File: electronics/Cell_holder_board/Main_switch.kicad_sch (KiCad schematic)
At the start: 0 parts

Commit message: Wiring diagram for mainswitch done
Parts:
- added BT5: Battery_Cell, symbol Device:Battery_Cell
- added Q1, Q2: IRLB8721PBF, Package_TO_SOT_THT:TO-220-3_Vertical, symbol Transistor_FET:IRLB8721PBF
- added R1: 1k, symbol Device:R
- added R2: 47k, symbol Device:R
- added R3: 4.7k, symbol Device:R
- added U1: LTV-817, Package_DIP:DIP-4_W7.62mm, symbol Isolator:LTV-817
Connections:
- new net: Q1.1 (G), Q2.1 (G), R2.1, U1.3
- new net: Q1.3 (S), Q2.3 (S), R2.2
- new net: R3.2, U1.2
- new net: R1.2, U1.4
- new net Arduino_mainswitch_gpio: U1.1
- new net GND: BT5.2 (-), Q1.2 (D), R3.1
- new net Load_minus: Q2.2 (D)
- new net Load_plus: BT5.1 (+), R1.1

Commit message: discord session with Johannes and Fabian, Schematic nearly done, all footprints fields filled
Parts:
- removed BT5: Battery_Cell, symbol Device:Battery_Cell
- added D1: 20V, Diode_SMD:D_SMA, symbol Device:D_TVS
- R1, R2, R3: footprint (none) -> Resistor_SMD:R_0805_2012Metric
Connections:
- net GND: now also D1.2 (A2)
- net Load_minus renamed Switch
- net Switch: now also D1.1 (A1)
- net Load_plus renamed U_Batt
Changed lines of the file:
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@@
 (kicad_sch (version 20230121) (generator eeschema)
   (paper "A4")
-  (junction (at 139.7 54.61) (diameter 0) (color 0 0 0 0)
-  )
   (junction (at 111.76 69.85) (diameter 0) (color 0 0 0 0)
   )
-  (junction (at 182.88 54.61) (diameter 0) (color 0 0 0 0)
+  (junction (at 139.7 93.98) (diameter 0) (color 0 0 0 0)
   )
   (junction (at 111.76 78.74) (diameter 0) (color 0 0 0 0)
   )
+  (junction (at 139.7 64.77) (diameter 0) (color 0 0 0 0)
+  )
   (junction (at 139.7 78.74) (diameter 0) (color 0 0 0 0)
   )
-  (wire (pts (xy 139.7 93.98) (xy 139.7 113.03))
-    (stroke (width 0) (type default))
-  )
   (wire (pts (xy 111.76 69.85) (xy 111.76 60.96))
     (stroke (width 0) (type default))
@@
     (stroke (width 0) (type default))
   )
+  (wire (pts (xy 158.75 93.98) (xy 139.7 93.98))
+    (stroke (width 0) (type default))
+  )
   (wire (pts (xy 139.7 78.74) (xy 139.7 83.82))
     (stroke (width 0) (type default))
@@
     (stroke (width 0) (type default))
   )
-  (wire (pts (xy 182.88 54.61) (xy 182.88 36.83))
+  (wire (pts (xy 158.75 74.93) (xy 158.75 64.77))
     (stroke (width 0) (type default))
   )
@@
     (stroke (width 0) (type default))
   )
+  (wire (pts (xy 139.7 93.98) (xy 139.7 101.6))
+    (stroke (width 0) (type default))
+  )
   (wire (pts (xy 111.76 78.74) (xy 111.76 88.9))
     (stroke (width 0) (type default))
   )
-  (wire (pts (xy 182.88 54.61) (xy 182.88 113.03))
-    (stroke (width 0) (type default))
-  )
   (wire (pts (xy 132.08 69.85) (xy 111.76 69.85))
     (stroke (width 0) (type default))
@@
     (stroke (width 0) (type default))
   )
-  (wire (pts (xy 166.37 54.61) (xy 139.7 54.61))
-    (stroke (width 0) (type default))
-  )
   (wire (pts (xy 106.68 36.83) (xy 106.68 44.45))
     (stroke (width 0) (type default))
   )
-  (wire (pts (xy 173.99 54.61) (xy 182.88 54.61))
-    (stroke (width 0) (type default))
-  )
   (wire (pts (xy 139.7 54.61) (xy 139.7 64.77))
     (stroke (width 0) (type default))
   )
-  (wire (pts (xy 139.7 113.03) (xy 143.51 113.03))
-    (stroke (width 0) (type default))
-  )
   (wire (pts (xy 111.76 88.9) (xy 132.08 88.9))
     (stroke (width 0) (type default))
   )
-  (wire (pts (xy 106.68 36.83) (xy 182.88 36.83))
-    (stroke (width 0) (type default))
-  )
   (wire (pts (xy 111.76 69.85) (xy 111.76 78.74))
     (stroke (width 0) (type default))
@@
     (stroke (width 0) (type default))
   )
+  (wire (pts (xy 158.75 64.77) (xy 139.7 64.77))
+    (stroke (width 0) (type default))
+  )
+  (wire (pts (xy 158.75 82.55) (xy 158.75 93.98))
+    (stroke (width 0) (type default))
+  )
   (wire (pts (xy 124.46 78.74) (xy 139.7 78.74))
     (stroke (width 0) (type default))
@@
     (stroke (width 0) (type default))
   )
-  (global_label "Load_minus" (shape input) (at 143.51 113.03 0) (fields_autoplaced)
-    (effects (font (size 1.27 1.27)) (justify left))
-    (property "Intersheetrefs" "${INTERSHEET_REFS}" (at 157.4827 113.03 0)
-      (effects (font (size 1.27 1.27)) (justify left) hide)
-    )
-  )
-  (global_label "Load_plus" (shape input) (at 182.88 113.03 180) (fields_autoplaced)
+  (hierarchical_label "Switch" (shape input) (at 139.7 101.6 270) (fields_autoplaced)
     (effects (font (size 1.27 1.27)) (justify right))
-    (property "Intersheetrefs" "${INTERSHEET_REFS}" (at 170.5402 113.03 0)
-      (effects (font (size 1.27 1.27)) (justify right) hide)
-    )
   )
   (hierarchical_label "Arduino_mainswitch_gpio" (shape input) (at 74.93 48.26 180) (fields_autoplaced)
     (effects (font (size 1.27 1.27)) (justify right))
   )
+  (hierarchical_label "U_Batt" (shape input) (at 106.68 36.83 90) (fields_autoplaced)
+    (effects (font (size 1.27 1.27)) (justify left))
+  )
   (symbol (lib_id "Device:R") (at 120.65 78.74 90) (unit 1)
-    (in_bom yes) (on_board yes) (dnp no) (fields_autoplaced)
+    (in_bom yes) (on_board yes) (dnp no)
     (property "Reference" "R2" (at 120.65 74.93 90)
       (effects (font (size 1.27 1.27)))
     )
-    (property "Value" "47k" (at 120.65 77.47 90)
-      (effects (font (size 1.27 1.27)))
-    )
-    (property "Footprint" "" (at 120.65 80.518 90)
+    (property "Value" "47k" (at 120.65 78.74 90)
+      (effects (font (size 1.27 1.27)))
+    )
+    (property "Footprint" "Resistor_SMD:R_0805_2012Metric" (at 120.65 80.518 90)
       (effects (font (size 1.27 1.27)) hide)
     )
@@
         (path "/c2697d40-f04f-4888-9ae9-ce0b7f222632/58237fb8-3152-4ac3-938c-94583c912e78"
           (reference "R2") (unit 1)
+        )
+      )
+    )
+  )
+  (symbol (lib_id "Device:D_TVS") (at 158.75 78.74 90) (unit 1)
+    (in_bom yes) (on_board yes) (dnp no) (fields_autoplaced)
+    (property "Reference" "D1" (at 161.29 78.105 90)
+      (effects (font (size 1.27 1.27)) (justify right))
+    )
+    (property "Value" "20V" (at 161.29 80.645 90)
+      (effects (font (size 1.27 1.27)) (justify right))
+    )
+    (property "Footprint" "Diode_SMD:D_SMA" (at 158.75 78.74 0)
+      (effects (font (size 1.27 1.27)) hide)
+    )
+    (property "Datasheet" "~" (at 158.75 78.74 0)
+      (effects (font (size 1.27 1.27)) hide)
+    )
+    (pin "1")
+    (pin "2")
+    (instances
+      (project "Cell_holder_board"
+        (path "/c2697d40-f04f-4888-9ae9-ce0b7f222632/58237fb8-3152-4ac3-938c-94583c912e78"
+          (reference "D1") (unit 1)
         )
       )
@@
     )
   )
-  (symbol (lib_id "Device:Battery_Cell") (at 168.91 54.61 270) (unit 1)
-    (in_bom yes) (on_board yes) (dnp no) (fields_autoplaced)
-    (property "Reference" "BT5" (at 170.942 48.26 90)
-      (effects (font (size 1.27 1.27)))
-    )
-    (property "Value" "Battery_Cell" (at 170.942 50.8 90)
-      (effects (font (size 1.27 1.27)))
-    )
-    (property "Footprint" "" (at 170.434 54.61 90)
-      (effects (font (size 1.27 1.27)) hide)
-    )
-    (property "Datasheet" "~" (at 170.434 54.61 90)
-      (effects (font (size 1.27 1.27)) hide)
-    )
-    (pin "1")
-    (pin "2")
-    (instances
-      (project "Cell_holder_board"
-        (path "/c2697d40-f04f-4888-9ae9-ce0b7f222632/58237fb8-3152-4ac3-938c-94583c912e78"
-          (reference "BT5") (unit 1)
-        )
-      )
-    )
-  )
   (symbol (lib_id "Isolator:LTV-817") (at 92.71 58.42 0) (unit 1)
     (in_bom yes) (on_board yes) (dnp no) (fields_autoplaced)
@@
   )
   (symbol (lib_id "Device:R") (at 73.66 60.96 90) (unit 1)
-    (in_bom yes) (on_board yes) (dnp no) (fields_autoplaced)
+    (in_bom yes) (on_board yes) (dnp no)
     (property "Reference" "R3" (at 73.66 57.15 90)
       (effects (font (size 1.27 1.27)))
     )
-    (property "Value" "4.7k" (at 73.66 59.69 90)
-      (effects (font (size 1.27 1.27)))
-    )
-    (property "Footprint" "" (at 73.66 62.738 90)
+    (property "Value" "4.7k" (at 73.66 60.96 90)
+      (effects (font (size 1.27 1.27)))
+    )
+    (property "Footprint" "Resistor_SMD:R_0805_2012Metric" (at 73.66 62.738 90)
       (effects (font (size 1.27 1.27)) hide)
     )
@@
   )
   (symbol (lib_id "Device:R") (at 106.68 48.26 0) (unit 1)
-    (in_bom yes) (on_board yes) (dnp no) (fields_autoplaced)
+    (in_bom yes) (on_board yes) (dnp no)
     (property "Reference" "R1" (at 109.22 47.625 0)
       (effects (font (size 1.27 1.27)) (justify left))
     )
-    (property "Value" "1k" (at 109.22 50.165 0)
-      (effects (font (size 1.27 1.27)) (justify left))
-    )
-    (property "Footprint" "" (at 104.902 48.26 90)
-      (effects (font (size 1.27 1.27)) hide)
-    )
+    (property "Value" "1k" (at 106.68 49.53 90)
+      (effects (font (size 1.27 1.27)) (justify left))
+    )
+    (property "Footprint" "Resistor_SMD:R_0805_2012Metric" (at 104.902 48.26 90)
+      (effects (font (size 1.27 1.27)) hide)
+    )

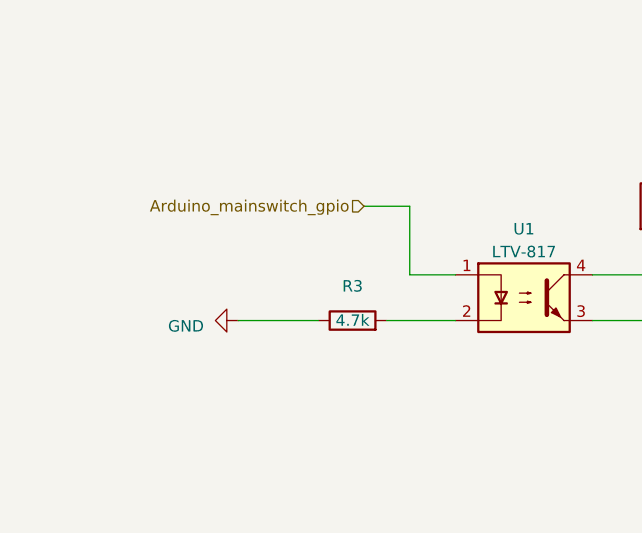
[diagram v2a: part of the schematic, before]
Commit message: finished layout of cell_holder_board
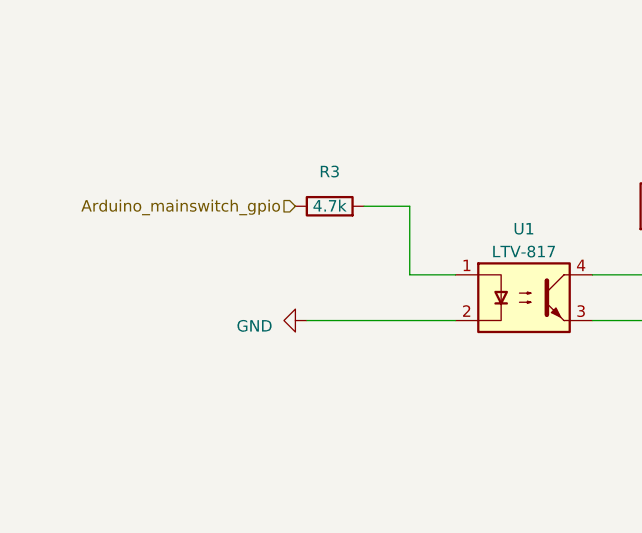
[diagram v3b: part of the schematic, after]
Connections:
- net Arduino_mainswitch_gpio: now also R3.1; no longer U1.1
- net GND: now also U1.2; no longer R3.1
- net at R3.2: now also U1.1; no longer U1.2
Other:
- moved on the sheet: R3
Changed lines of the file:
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@@
     (stroke (width 0) (type default))
   )
-  (wire (pts (xy 77.47 60.96) (xy 85.09 60.96))
+  (wire (pts (xy 68.58 60.96) (xy 85.09 60.96))
     (stroke (width 0) (type default))
   )
@@
   )
   (wire (pts (xy 111.76 69.85) (xy 111.76 78.74))
-    (stroke (width 0) (type default))
-  )
-  (wire (pts (xy 60.96 60.96) (xy 69.85 60.96))
     (stroke (width 0) (type default))
   )
@@
     (effects (font (size 1.27 1.27)) (justify right))
   )
-  (hierarchical_label "Arduino_mainswitch_gpio" (shape input) (at 74.93 48.26 180) (fields_autoplaced)
+  (hierarchical_label "Arduino_mainswitch_gpio" (shape input) (at 67.31 48.26 180) (fields_autoplaced)
     (effects (font (size 1.27 1.27)) (justify right))
   )
@@
     )
   )
-  (symbol (lib_id "power:GND") (at 60.96 60.96 270) (unit 1)
-    (in_bom yes) (on_board yes) (dnp no) (fields_autoplaced)
-    (property "Reference" "#PWR02" (at 54.61 60.96 0)
-      (effects (font (size 1.27 1.27)) hide)
-    )
-    (property "Value" "GND" (at 57.15 61.595 90)
+  (symbol (lib_id "power:GND") (at 68.58 60.96 270) (unit 1)
+    (in_bom yes) (on_board yes) (dnp no) (fields_autoplaced)
+    (property "Reference" "#PWR02" (at 62.23 60.96 0)
+      (effects (font (size 1.27 1.27)) hide)
+    )
+    (property "Value" "GND" (at 64.77 61.595 90)
       (effects (font (size 1.27 1.27)) (justify right))
     )
-    (property "Footprint" "" (at 60.96 60.96 0)
-      (effects (font (size 1.27 1.27)) hide)
-    )
-    (property "Datasheet" "" (at 60.96 60.96 0)
+    (property "Footprint" "" (at 68.58 60.96 0)
+      (effects (font (size 1.27 1.27)) hide)
+    )
+    (property "Datasheet" "" (at 68.58 60.96 0)
       (effects (font (size 1.27 1.27)) hide)
     )
@@
     )
   )
-  (symbol (lib_id "Device:R") (at 73.66 60.96 90) (unit 1)
+  (symbol (lib_id "Device:R") (at 71.12 48.26 90) (unit 1)
     (in_bom yes) (on_board yes) (dnp no)
-    (property "Reference" "R3" (at 73.66 57.15 90)
-      (effects (font (size 1.27 1.27)))
-    )
-    (property "Value" "4.7k" (at 73.66 60.96 90)
-      (effects (font (size 1.27 1.27)))
-    )
-    (property "Footprint" "Resistor_SMD:R_0805_2012Metric" (at 73.66 62.738 90)
-      (effects (font (size 1.27 1.27)) hide)
-    )
-    (property "Datasheet" "~" (at 73.66 60.96 0)
-      (effects (font (size 1.27 1.27)) hide)
-    )
+    (property "Reference" "R3" (at 71.12 44.45 90)
+      (effects (font (size 1.27 1.27)))
+    )
+    (property "Value" "4.7k" (at 71.12 48.26 90)
+      (effects (font (size 1.27 1.27)))
+    )
+    (property "Footprint" "Resistor_SMD:R_0805_2012Metric" (at 71.12 50.038 90)
+      (effects (font (size 1.27 1.27)) hide)
+    )
+    (property "Datasheet" "~" (at 71.12 48.26 0)
+      (effects (font (size 1.27 1.27)) hide)
+    )
